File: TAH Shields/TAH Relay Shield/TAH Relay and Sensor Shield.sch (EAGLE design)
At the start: 38 parts, among them T1 2N3904, T2 2N3904

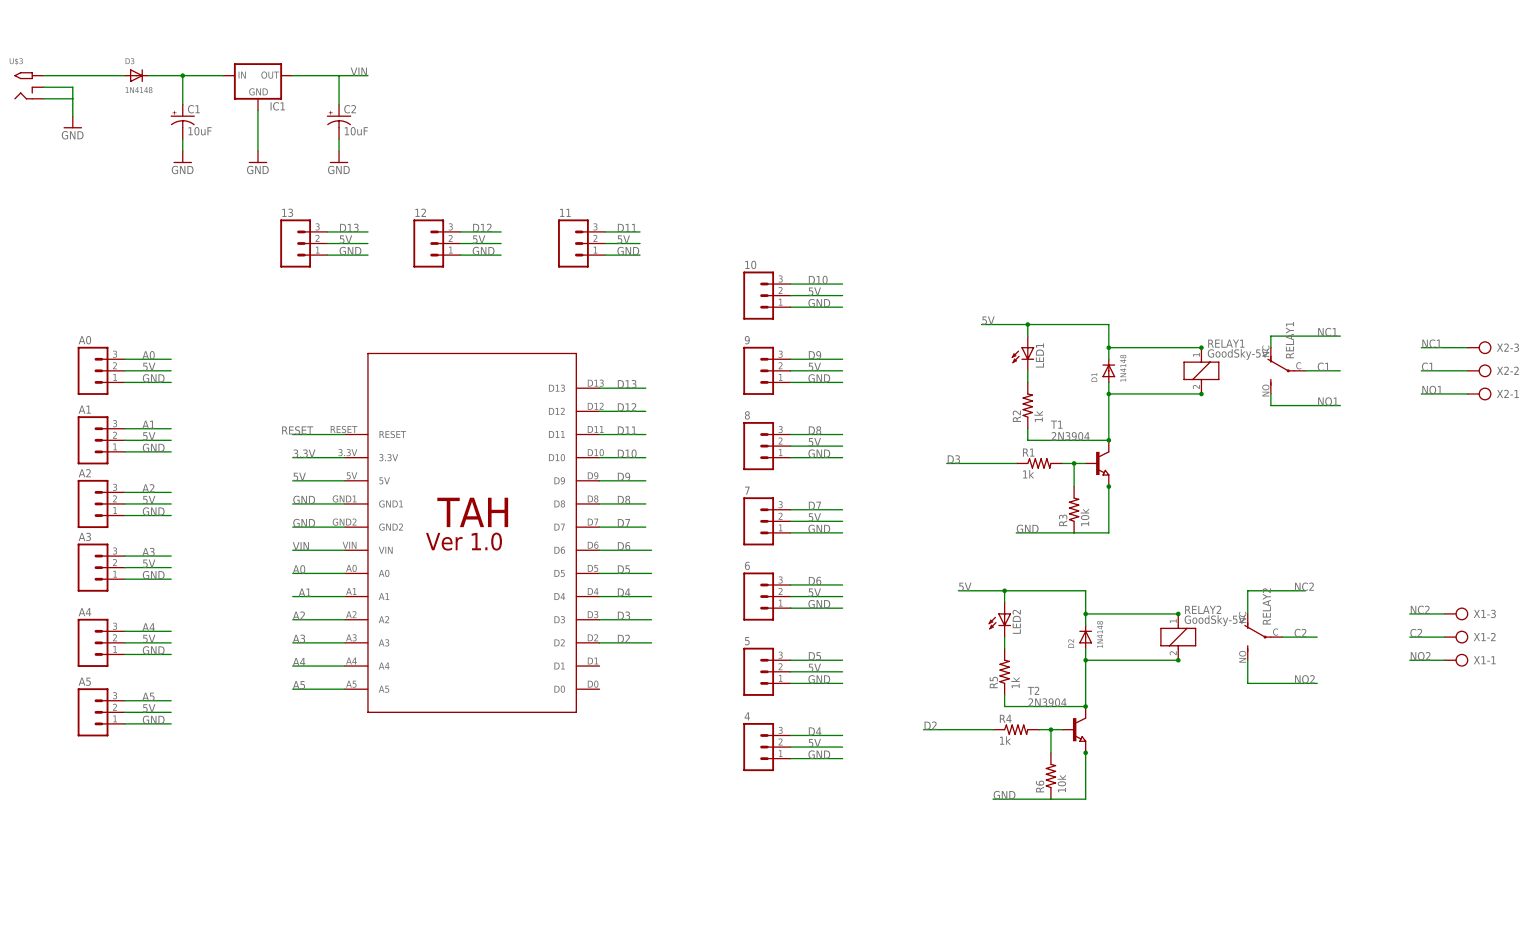
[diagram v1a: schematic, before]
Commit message: All shields updated with latest Tah footprint
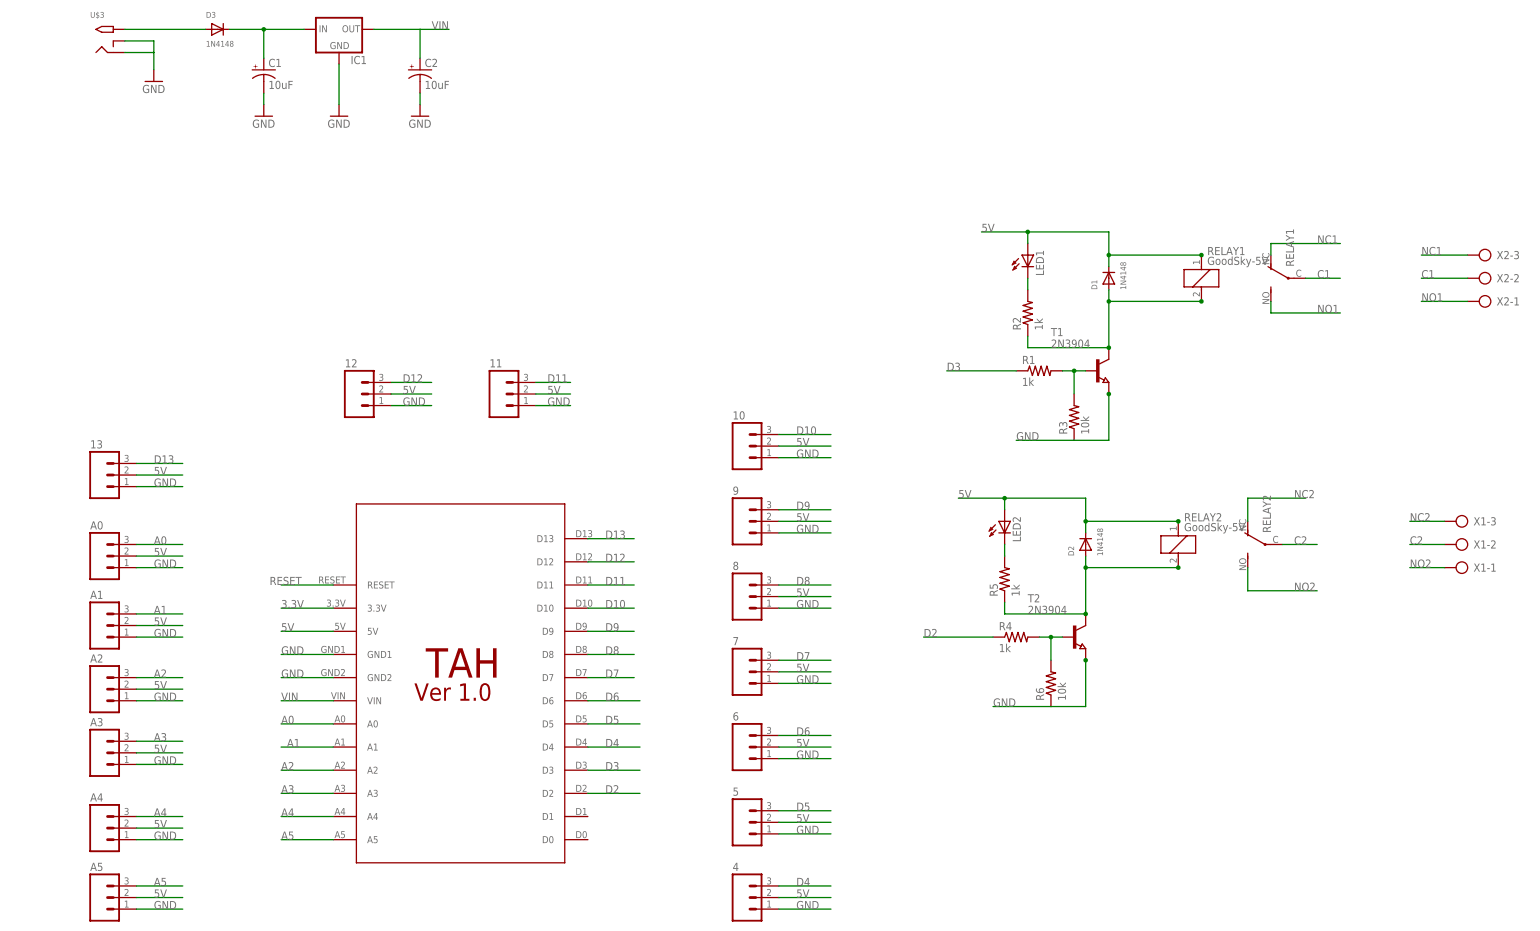
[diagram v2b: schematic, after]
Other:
- moved on the sheet: 10, 11, 12, 13, 4, 5, 6, 7, 8, 9, A0, A1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
